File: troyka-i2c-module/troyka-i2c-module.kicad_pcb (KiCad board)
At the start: 2 copper layers, 25.4 x 25.4 mm, 5 parts, among them J1 UP (A), J2 DOWN (A)

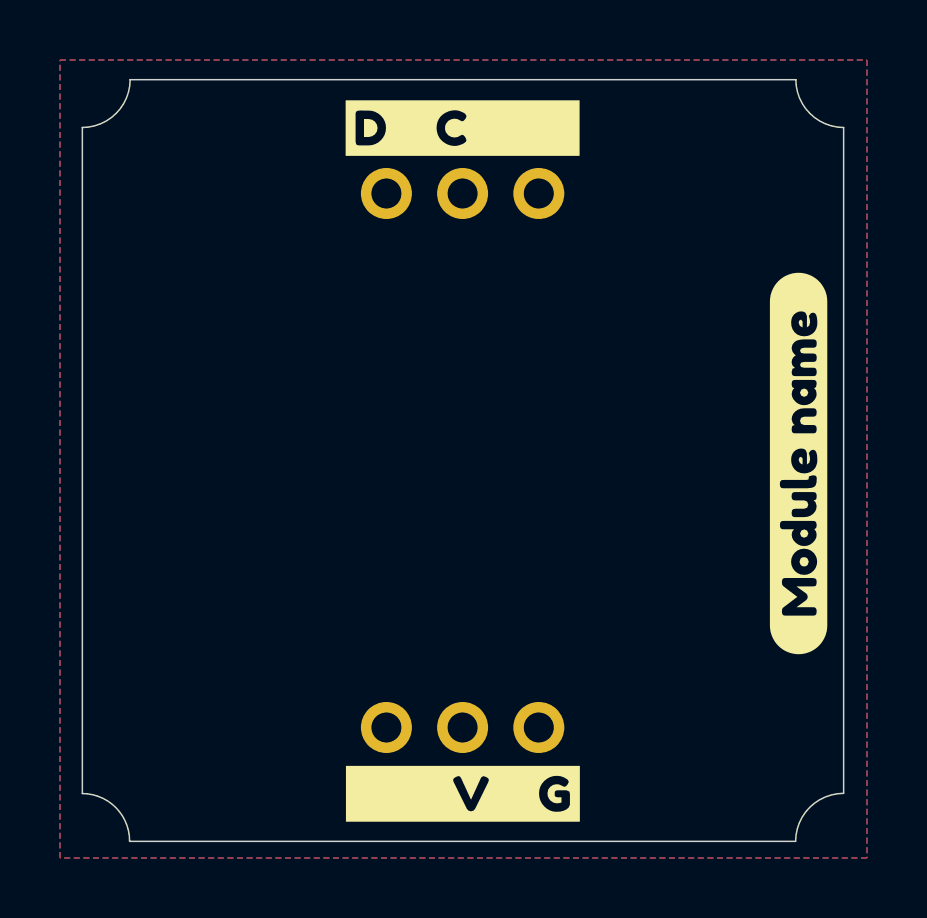
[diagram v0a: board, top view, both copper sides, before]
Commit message: Update templates and CI
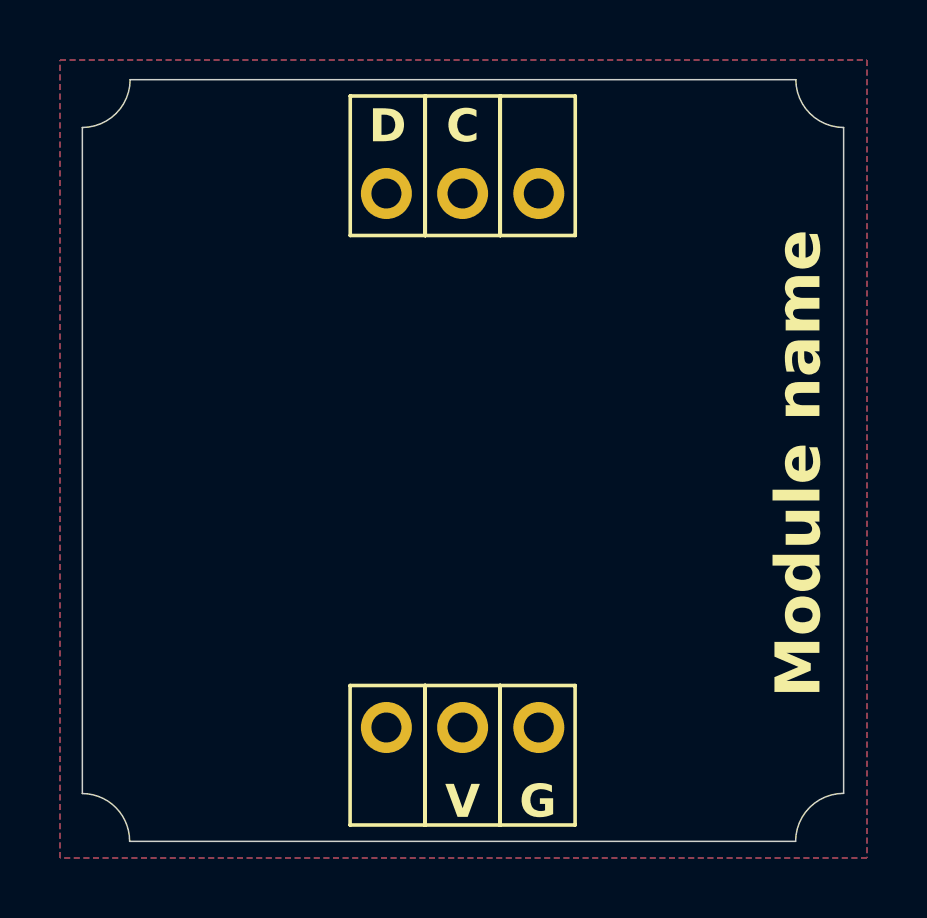
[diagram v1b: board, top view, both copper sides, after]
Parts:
- removed kibuzzard-63E392E0: G***, kibuzzard-63E392E0
- removed kibuzzard-63E394FC: G***, kibuzzard-63E394FC
- removed kibuzzard-63E39575: G***, kibuzzard-63E39575
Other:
- board text added: "C"
- board text added: "D"
- board text added: "G"
- board text added: "Module name"
- board text added: "V"
